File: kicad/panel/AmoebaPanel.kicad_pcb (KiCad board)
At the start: 2 copper layers, 127.8 x 100 mm, 204 parts, among them J1 Conn_01x01_Pin, J2 Conn_01x01_Pin, J3 Conn_01x01_Pin, J4 Conn_01x01_Pin, SW1 SW_SPST

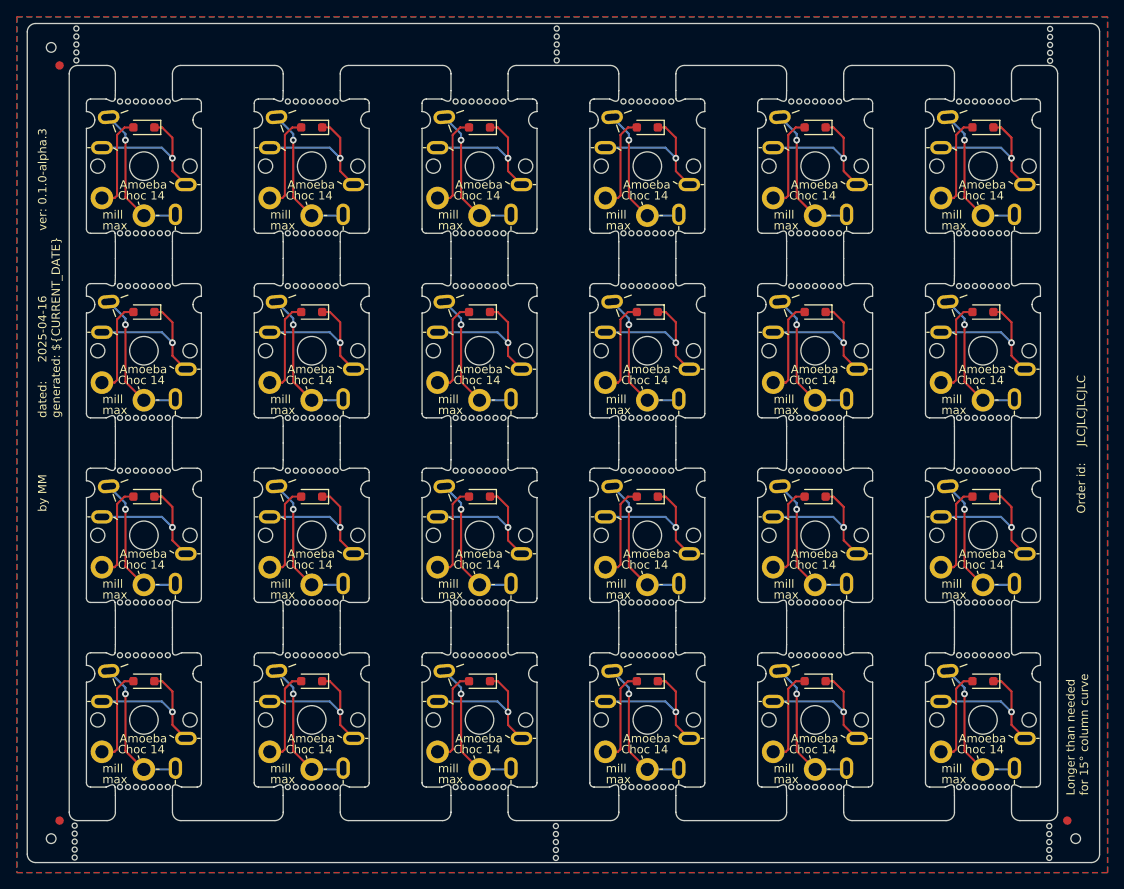
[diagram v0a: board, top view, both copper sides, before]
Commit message: feat(panel): fix silk typo, add art, bump version
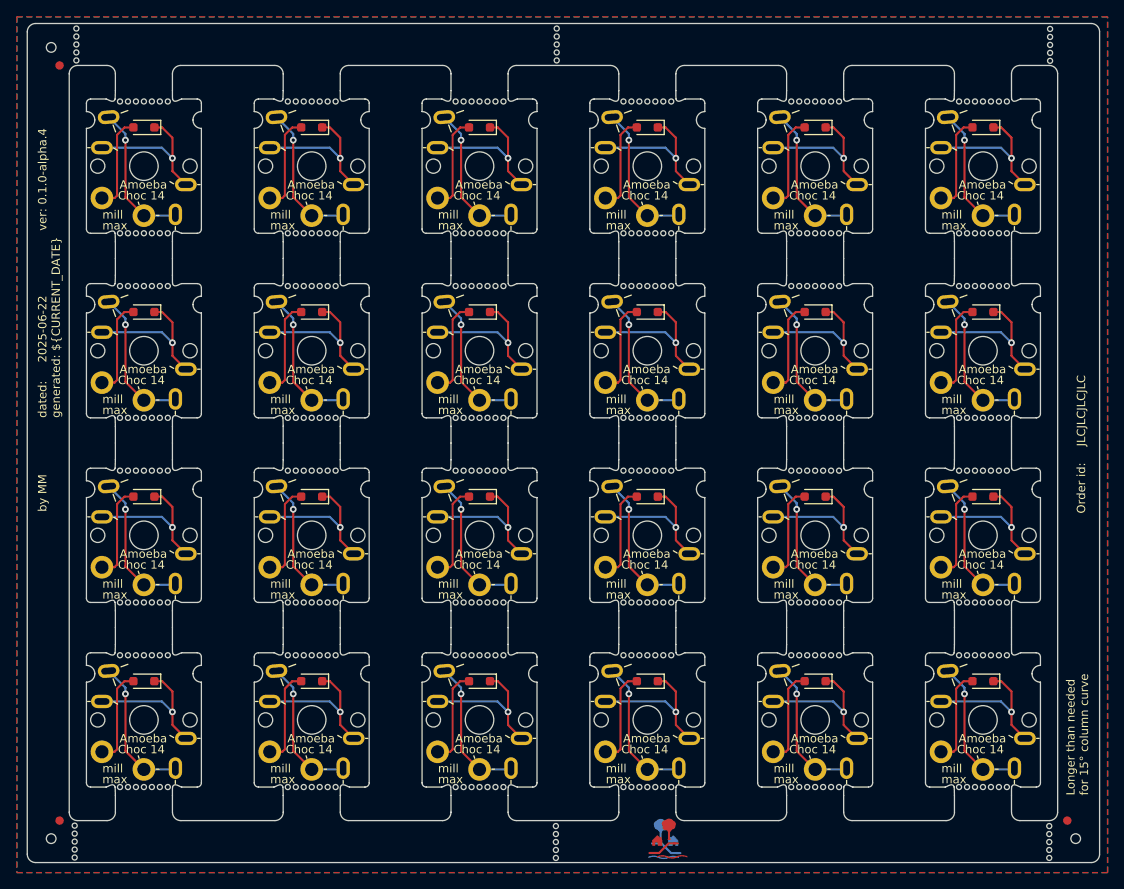
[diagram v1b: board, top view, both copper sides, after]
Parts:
- added ?: , , F.Cu at (172.4, 149.7)
- added ?: , , F.Cu at (171.7, 150.2)
- added ?: , , F.Cu at (171.5, 150.1)
- added ?: , , F.Cu at (172.1, 148.5)
- added REF**: art_tree, Dactyl:art_tree, F.Cu at (171.7, 147.2)
- added REF**: art_house, Dactyl:art_house, F.Cu at (170.3, 148.0)
- added REF**: art_house, Dactyl:art_house, B.Cu at (172.3, 148.1)
- added REF**: art_tree, Dactyl:art_tree, B.Cu at (170.7, 147.2)

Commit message: feat(panel): updated amoeba
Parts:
- removed the D1 at (209.2, 129.2)
- removed the D1 at (209.2, 85.2)
- removed the D1 at (169.2, 129.2)
- removed the D1 at (149.2, 85.2)
- removed the D1 at (169.2, 107.2)
- removed the D1 at (189.2, 63.2)
- removed the D1 at (109.2, 107.2)
- removed the D1 at (129.2, 85.2)
- removed the D1 at (209.2, 63.2)
- removed the D1 at (169.2, 63.2)
- removed the D1 at (149.2, 129.2)
- removed the D1 at (109.2, 129.2)
- removed the D1 at (109.2, 85.2)
- removed the D1 at (129.2, 63.2)
- removed the D1 at (109.2, 63.2)
- removed the D1 at (209.2, 107.2)
- removed the D1 at (149.2, 63.2)
- removed the D1 at (149.2, 107.2)
- removed the D1 at (189.2, 107.2)
- removed the D1 at (169.2, 85.2)
- removed the D1 at (129.2, 107.2)
- removed the D1 at (129.2, 129.2)
- removed the D1 at (189.2, 85.2)
- removed the D1 at (189.2, 129.2)
- added D1: 1N4148, Diode_SMD:D_SOD-123, F.Cu at (209.2, 107.1)
- added D1: 1N4148, Diode_SMD:D_SOD-123, F.Cu at (109.2, 63.1)
- added D1: 1N4148, Diode_SMD:D_SOD-123, F.Cu at (189.2, 85.1)
- added D1: 1N4148, Diode_SMD:D_SOD-123, F.Cu at (169.2, 107.1)
- added D1: 1N4148, Diode_SMD:D_SOD-123, F.Cu at (169.2, 85.1)
- added D1: 1N4148, Diode_SMD:D_SOD-123, F.Cu at (109.2, 85.1)
- added D1: 1N4148, Diode_SMD:D_SOD-123, F.Cu at (169.2, 129.1)
- added D1: 1N4148, Diode_SMD:D_SOD-123, F.Cu at (129.2, 107.1)
- added D1: 1N4148, Diode_SMD:D_SOD-123, F.Cu at (109.2, 129.1)
- added D1: 1N4148, Diode_SMD:D_SOD-123, F.Cu at (189.2, 63.1)
- added D1: 1N4148, Diode_SMD:D_SOD-123, F.Cu at (149.2, 107.1)
- added D1: 1N4148, Diode_SMD:D_SOD-123, F.Cu at (149.2, 63.1)
- added D1: 1N4148, Diode_SMD:D_SOD-123, F.Cu at (169.2, 63.1)
- added D1: 1N4148, Diode_SMD:D_SOD-123, F.Cu at (149.2, 129.1)
- added D1: 1N4148, Diode_SMD:D_SOD-123, F.Cu at (149.2, 85.1)
- added D1: 1N4148, Diode_SMD:D_SOD-123, F.Cu at (209.2, 85.1)
- added D1: 1N4148, Diode_SMD:D_SOD-123, F.Cu at (209.2, 63.1)
- added D1: 1N4148, Diode_SMD:D_SOD-123, F.Cu at (189.2, 107.1)
- added D1: 1N4148, Diode_SMD:D_SOD-123, F.Cu at (209.2, 129.1)
- added D1: 1N4148, Diode_SMD:D_SOD-123, F.Cu at (129.2, 129.1)
- added D1: 1N4148, Diode_SMD:D_SOD-123, F.Cu at (129.2, 85.1)
- added D1: 1N4148, Diode_SMD:D_SOD-123, F.Cu at (109.2, 107.1)
- added D1: 1N4148, Diode_SMD:D_SOD-123, F.Cu at (189.2, 129.1)
- added D1: 1N4148, Diode_SMD:D_SOD-123, F.Cu at (129.2, 63.1)
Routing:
- net Net-(D1-A): track 275.2 -> 270.6 mm
- net /row: track 423.0 -> 419.9 mm
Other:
- board text added: "v010a4"
- board text removed: "v010a3"
